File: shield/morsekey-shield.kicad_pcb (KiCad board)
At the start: 2 copper layers, 36.4 x 20.3 mm, 6 parts, among them J1 PinSocket_1x09_P2.54mm_Vertic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, J2 PinSocket_1x09_P2.54mm_Vertic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

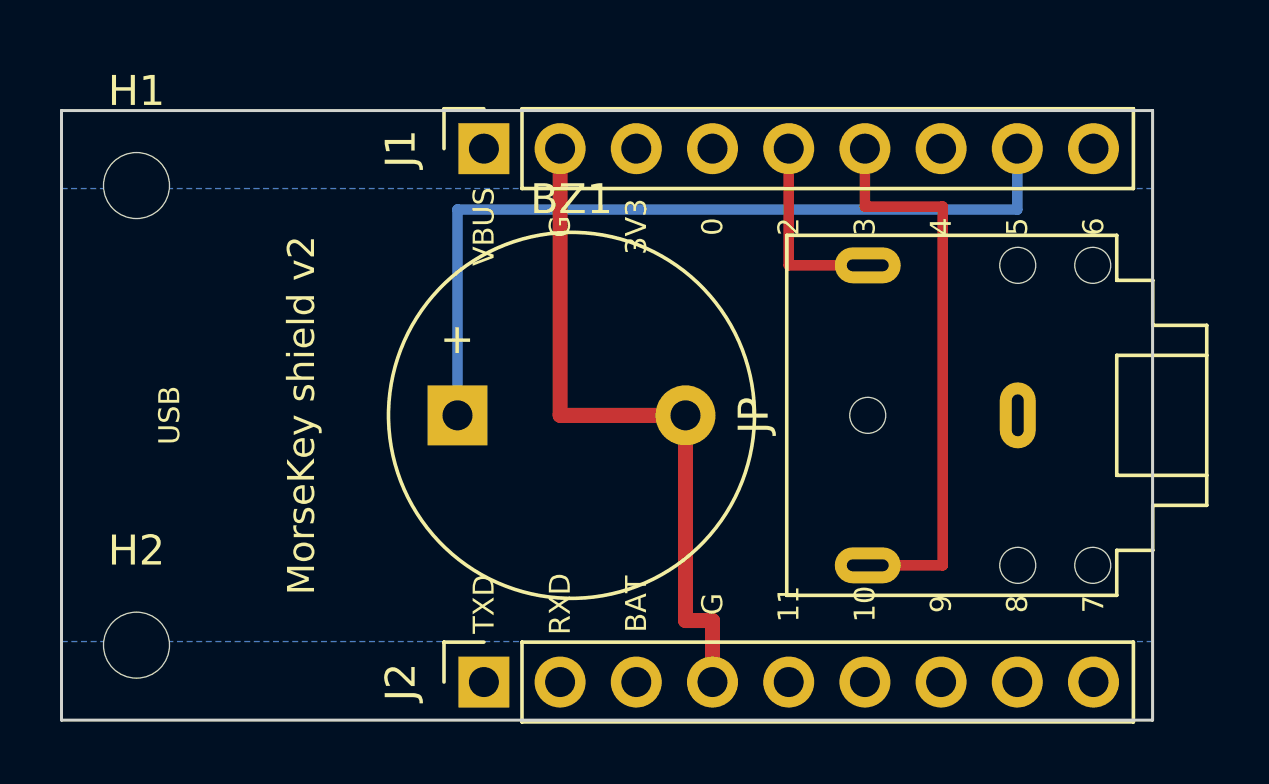
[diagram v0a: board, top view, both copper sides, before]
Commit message: Fix piezo footprint to real 5.0mm pitch; BOM with verified DigiKey parts
The RM7.6 footprint matched no purchasable part - every available 12mm
through-hole piezo transducer (TDK PS1240, Same Sky CPT-1206/1207) uses
5.0mm pin pitch. Swap to the TDK PS1240 footprint (1.0mm drills fit all
of them) and pin the BOM to in-stock DigiKey parts: jack CP1-3523N-ND,
piezo 2223-CPT-1207-5LTH-T-ND.

Co-Authored-By: Claude Fable 5 <noreply@anthropic.com>
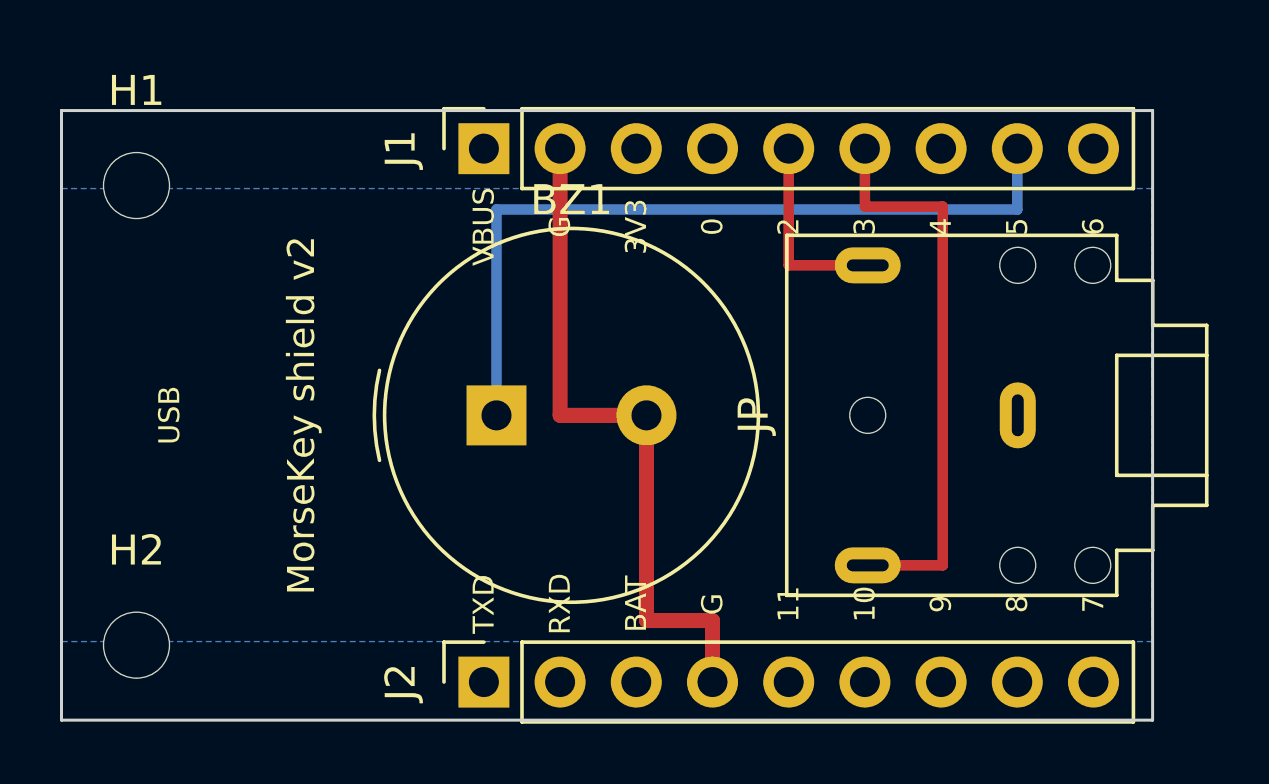
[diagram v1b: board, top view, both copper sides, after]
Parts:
- BZ1: value Buzzer_12x9.5RM7.6 -> Buzzer_TDK_PS1240P02BT_D12.2mm_H6.5mm; footprint Buzzer_12x9.5RM7.6 -> Buzzer_TDK_PS1240P02BT_D12.2mm_H6.5mm
- moved BZ1 1.30 mm to (14.5, 10.2)
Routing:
- net PIEZO: track 27.6 -> 26.2 mm
